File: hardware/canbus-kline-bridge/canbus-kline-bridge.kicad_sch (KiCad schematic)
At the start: 36 parts, among them J1 USB_B_Micro, J2 SWD, J4 CANBus, J5 CANBus, J6 K-Line, Q1 2N7002, Q2 2N7002, U1 MCP1754S-3302xCB, U2 STM32F042F6Px, U3 Voltage Regulator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

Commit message: Working on the kline bridge a bit more
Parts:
- removed JP1: CAN_RX/USB_D-, Connector_PinHeader_2.54mm:PinHeader_1x03_P2.54mm_Vertical, symbol Jumper:Jumper_3_Bridged12
- removed JP2: CAN_TX/USB_D+, Connector_PinHeader_2.54mm:PinHeader_1x03_P2.54mm_Vertical, symbol Jumper:Jumper_3_Bridged12
- added R5, R6, R7, R8: 10k, Resistor_SMD:R_0805_2012Metric_Pad1.20x1.40mm_HandSolder, symbol Device:R
- added U6: CY15E004J, Package_SO:SOIC-8_5.23x5.23mm_P1.27mm, symbol Beirdo:CY15E004J
- added U7: MCP2517FD, Package_SO:SOIC-14_3.9x8.7mm_P1.27mm, symbol Interface_CAN_LIN:MCP2517FD-xSL
- added X1: ASV-20.000MHZ-EJ-T, Oscillator:Oscillator_SMD_Abracon_ASV-4Pin_7.0x5.1mm, symbol Oscillator:ASV-xxxMHz
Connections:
- net +3V3: now also S1.2 (1), R5.1, R6.1, R7.1, R8.1, U6.8 (VCC), U7.14 (VDD), X1.1 (EN), X1.4 (Vdd)
- net CAN_RX: now also U7.2 (RXCAN)
- net CAN_TX: now also U7.1 (TXCAN)
- net GND: now also S2.2 (1), U6.2 (A1), U6.3 (A2), U6.4 (GND), U6.7 (WP), U7.7 (VSS), X1.2 (GND)
- net USB_D+: now also U2.18 (PA10/PA12)
- net USB_D-: now also U2.17 (PA9/PA11)
- net ~{RESET}: now also S2.4 (2)
- net Net-(R1-Pad1): now reaches S1.4 (2)
- net ~{SPI_SS}: now reaches U2.10 (PA4)
- net ~{SPI_SS}: now also R7.2, U7.13 (nCS)
- net SCK: now reaches U2.11 (PA5)
- net SCK: now also U7.10 (SCK)
- net MISO: now reaches U2.12 (PA6)
- net MISO: now also U7.12 (SDO)
- net MOSI: now reaches U2.13 (PA7)
- net MOSI: now also U7.11 (SDI)
- net ~{CAN_INT}: now reaches U2.7 (PA1)
- net ~{CAN_INT}: now also R8.2, U7.4 (~{INT})
- net SCL1 renamed SCL
- net SCL: now also R6.2, U6.6 (SCL)
- net SDA1 renamed SDA
- net SDA: now also R5.2, U6.5 (SDA)
- new net: U7.6 (OSC1), X1.3 (OUT)
- no-connect marks 7 -> 6
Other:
- note added: "I2C Addresses 0x50/51 - 0x56/57 Using 0x50/51"
- moved on the sheet: C2, C4, C5, C6, C7, F1, J1, J2, Q1, Q2, U1, U3

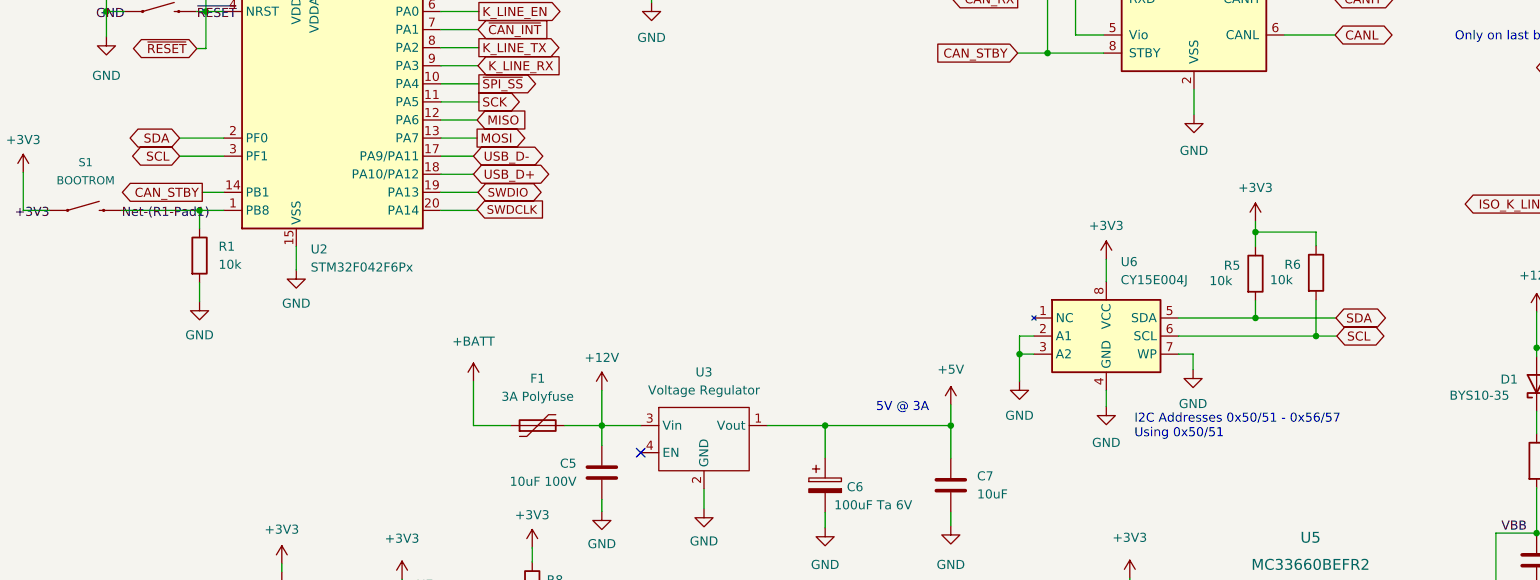
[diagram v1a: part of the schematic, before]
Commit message: Plumbed out the kline over canbus code
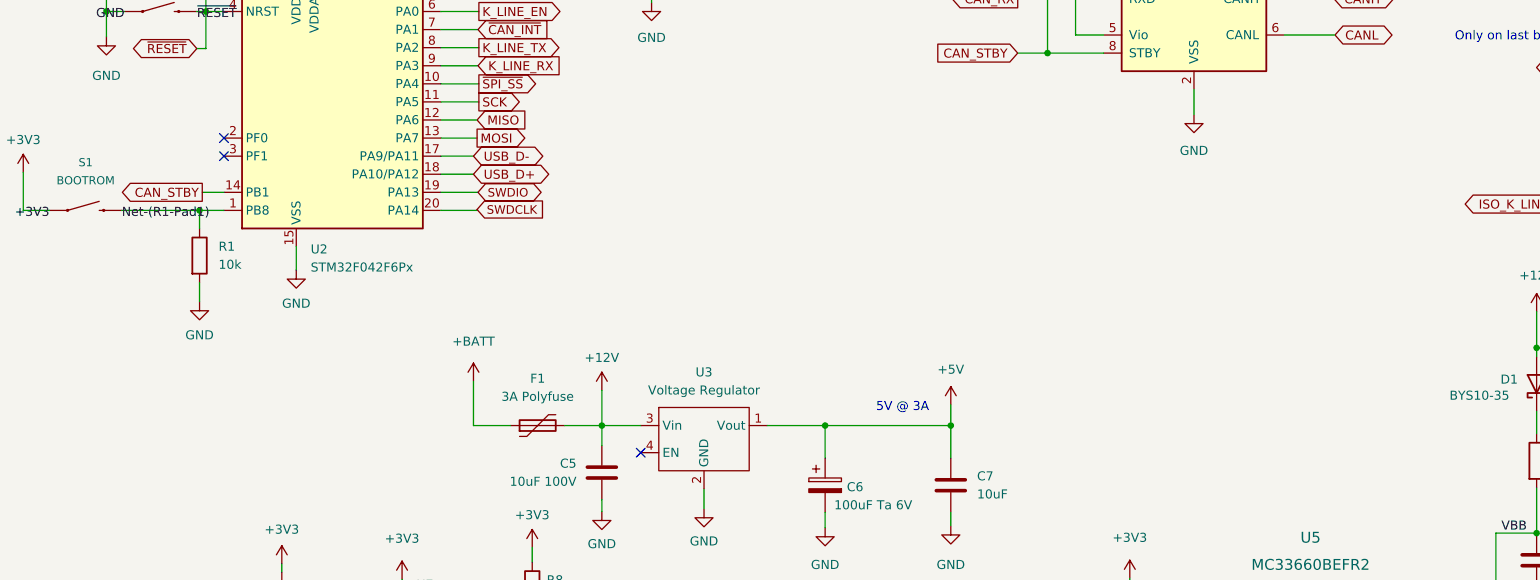
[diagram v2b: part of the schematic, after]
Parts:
- removed R5, R6: 10k, Resistor_SMD:R_0805_2012Metric_Pad1.20x1.40mm_HandSolder, symbol Device:R
- removed U6: CY15E004J, Package_SO:SOIC-8_5.23x5.23mm_P1.27mm, symbol Beirdo:CY15E004J
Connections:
- net SCL: no longer names the net of U2.3 (PF1)
- net SDA: no longer names the net of U2.2 (PF0)
- no-connect marks 6 -> 8
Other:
- note removed: "I2C Addresses 0x50/51 - 0x56/57 Using 0x50/51"
